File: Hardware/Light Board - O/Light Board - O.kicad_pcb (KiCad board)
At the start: 2 copper layers, 46.8 x 36.8 mm, 11 parts, among them J1 V+, J2 V-

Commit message: Finished all light boards
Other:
- board text added: "-"
- board text removed: "–"
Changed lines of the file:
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@@
 		)
 	)
-	(gr_text "–"
+	(gr_text "-"
 		(at 145.1 112.1 0)
 		(layer "F.SilkS")

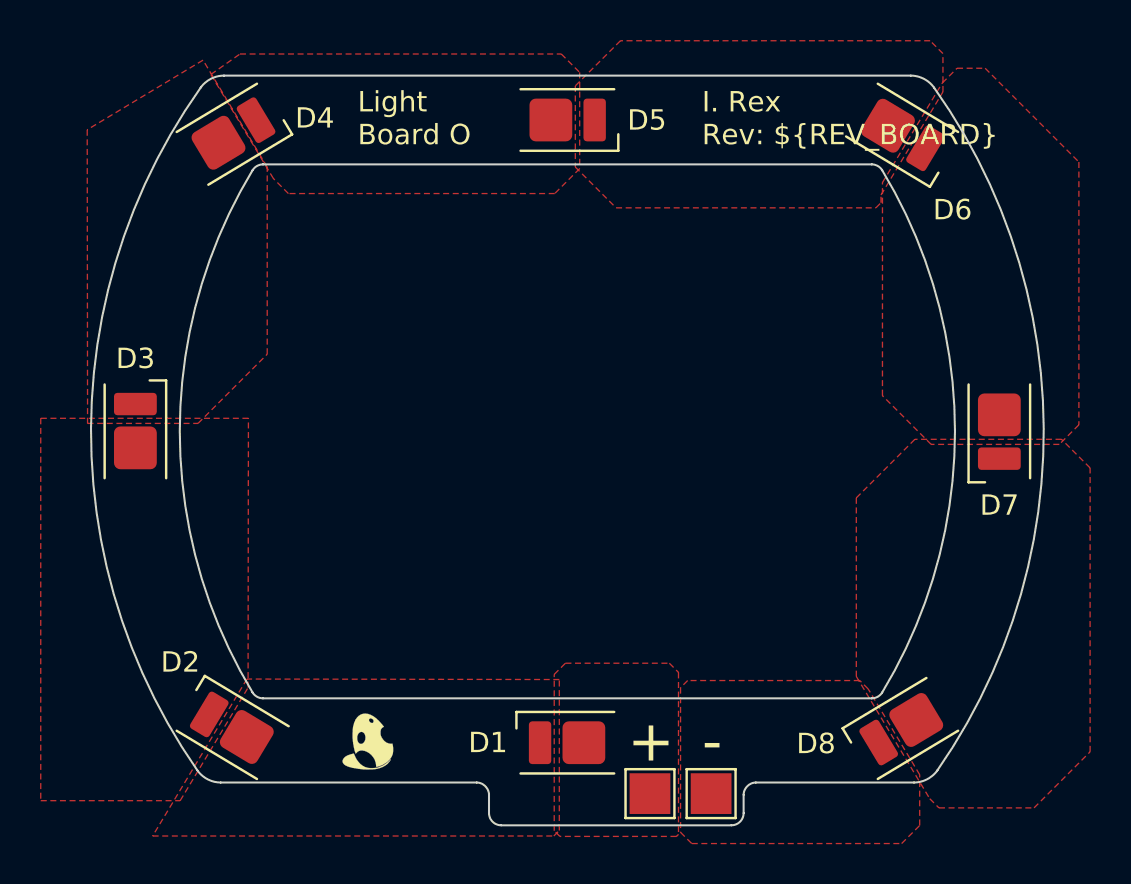
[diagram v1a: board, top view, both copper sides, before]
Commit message: Added LED library and fixed orientation
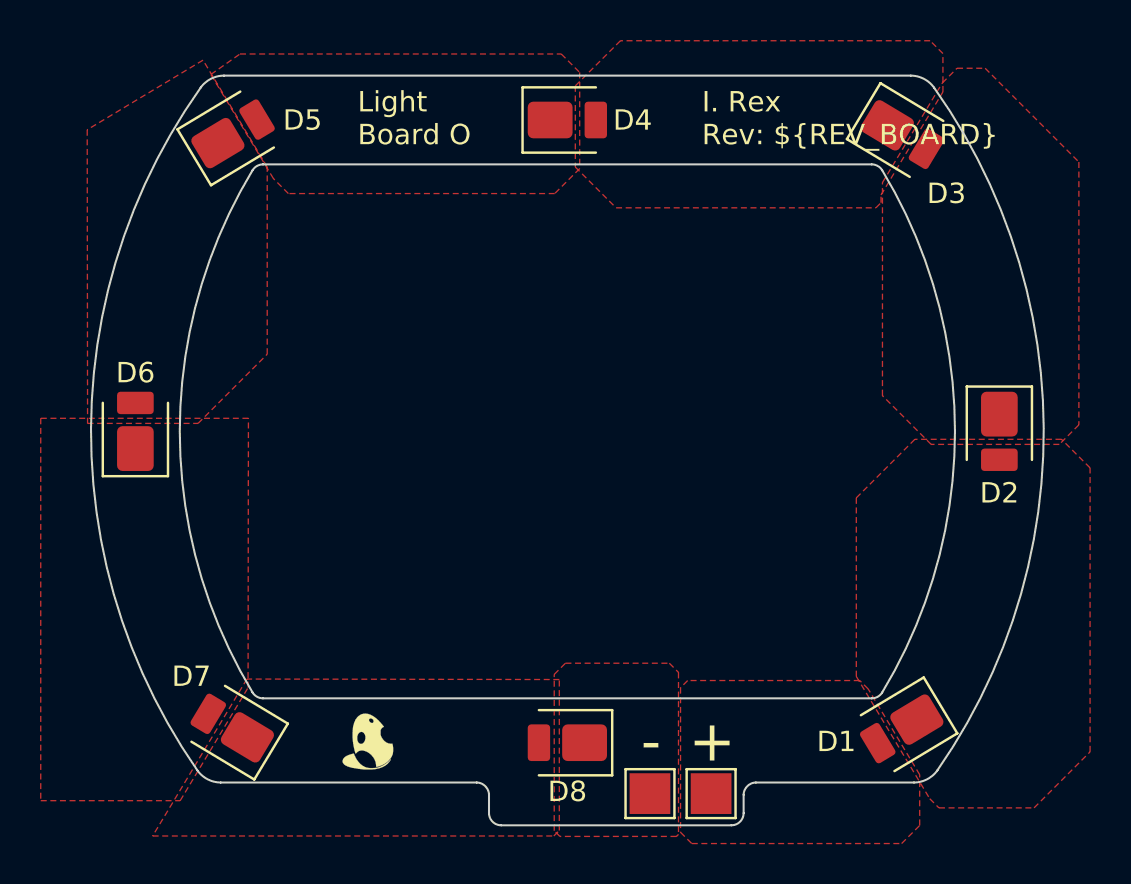
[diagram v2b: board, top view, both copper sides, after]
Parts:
- D1: renamed from D8; footprint LED_SMD:LED_Everlight-SMD3528_3.5x2.8mm_67-21ST -> irex_LED_SMD:LED_Cree_J-Series_SMD2835_2.8x3.5mm
- D2: renamed from D7; footprint LED_SMD:LED_Everlight-SMD3528_3.5x2.8mm_67-21ST -> irex_LED_SMD:LED_Cree_J-Series_SMD2835_2.8x3.5mm
- D3: renamed from D6; footprint LED_SMD:LED_Everlight-SMD3528_3.5x2.8mm_67-21ST -> irex_LED_SMD:LED_Cree_J-Series_SMD2835_2.8x3.5mm
- D4: renamed from D5; footprint LED_SMD:LED_Everlight-SMD3528_3.5x2.8mm_67-21ST -> irex_LED_SMD:LED_Cree_J-Series_SMD2835_2.8x3.5mm
- D5: renamed from D4; footprint LED_SMD:LED_Everlight-SMD3528_3.5x2.8mm_67-21ST -> irex_LED_SMD:LED_Cree_J-Series_SMD2835_2.8x3.5mm
- D6: renamed from D3; footprint LED_SMD:LED_Everlight-SMD3528_3.5x2.8mm_67-21ST -> irex_LED_SMD:LED_Cree_J-Series_SMD2835_2.8x3.5mm
- D7: renamed from D2; footprint LED_SMD:LED_Everlight-SMD3528_3.5x2.8mm_67-21ST -> irex_LED_SMD:LED_Cree_J-Series_SMD2835_2.8x3.5mm
- D8: renamed from D1; footprint LED_SMD:LED_Everlight-SMD3528_3.5x2.8mm_67-21ST -> irex_LED_SMD:LED_Cree_J-Series_SMD2835_2.8x3.5mm
- J1: renamed from J2; value V- -> V+
- J2: renamed from J1; value V+ -> V-
- turned D1 to -149 degrees
- turned D2 to -90 degrees
- turned D3 to -31 degrees
- turned D4 to 0 degrees
- turned D5 to 31 degrees
- turned D6 to 90 degrees
- turned D7 to 149 degrees
- turned D8 to 180 degrees
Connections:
- D1 pad 1: /V- -> /K_D1
- D1 pad 2: /K_D7 -> /V+
- D2 pad 1: /K_D7 -> /K_D2
- D2 pad 2: /K_D6 -> /K_D1
- D3 pad 1: /K_D6 -> /K_D3
- D3 pad 2: /K_D5 -> /K_D2
- D4 pad 1: /K_D5 -> /K_D4
- D4 pad 2: /K_D4 -> /K_D3
- D5 pad 1: /K_D4 -> /K_D5
- D5 pad 2: /K_D3 -> /K_D4
- D6 pad 1: /K_D3 -> /K_D6
- D6 pad 2: /K_D2 -> /K_D5
- D7 pad 1: /K_D2 -> /K_D7
- D7 pad 2: /K_D1 -> /K_D6
- D8 pad 1: /K_D1 -> /V-
- D8 pad 2: /V+ -> /K_D7
- J1 pad 1: /V- -> /V+
- J2 pad 1: /V+ -> /V-
